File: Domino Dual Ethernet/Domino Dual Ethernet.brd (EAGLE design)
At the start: 45.7 x 33 mm, 47 parts, among them J1 HL-59T-2X1, J2 MH18-1, J3 MH18-1

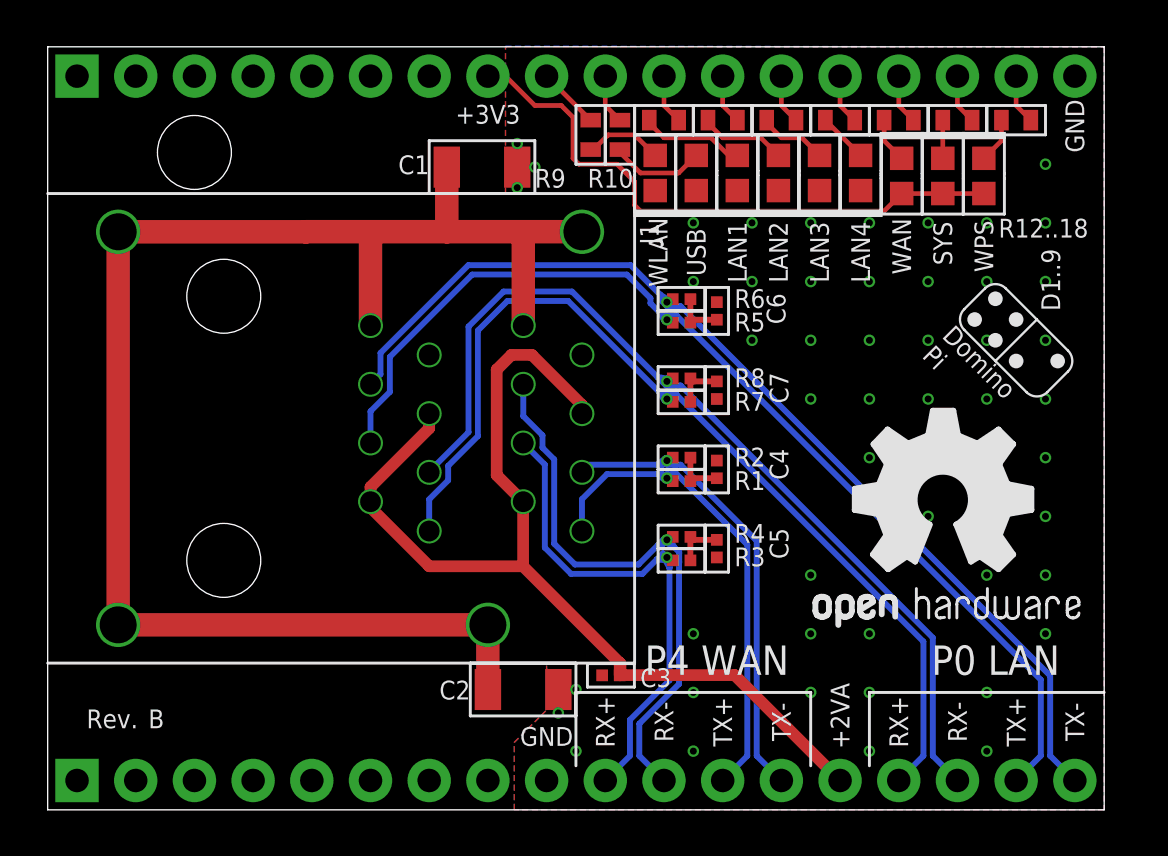
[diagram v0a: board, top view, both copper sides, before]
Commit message: Domino Dual Ethernet Rev. C: Changed dual Magjack connector for new one, changed Logos
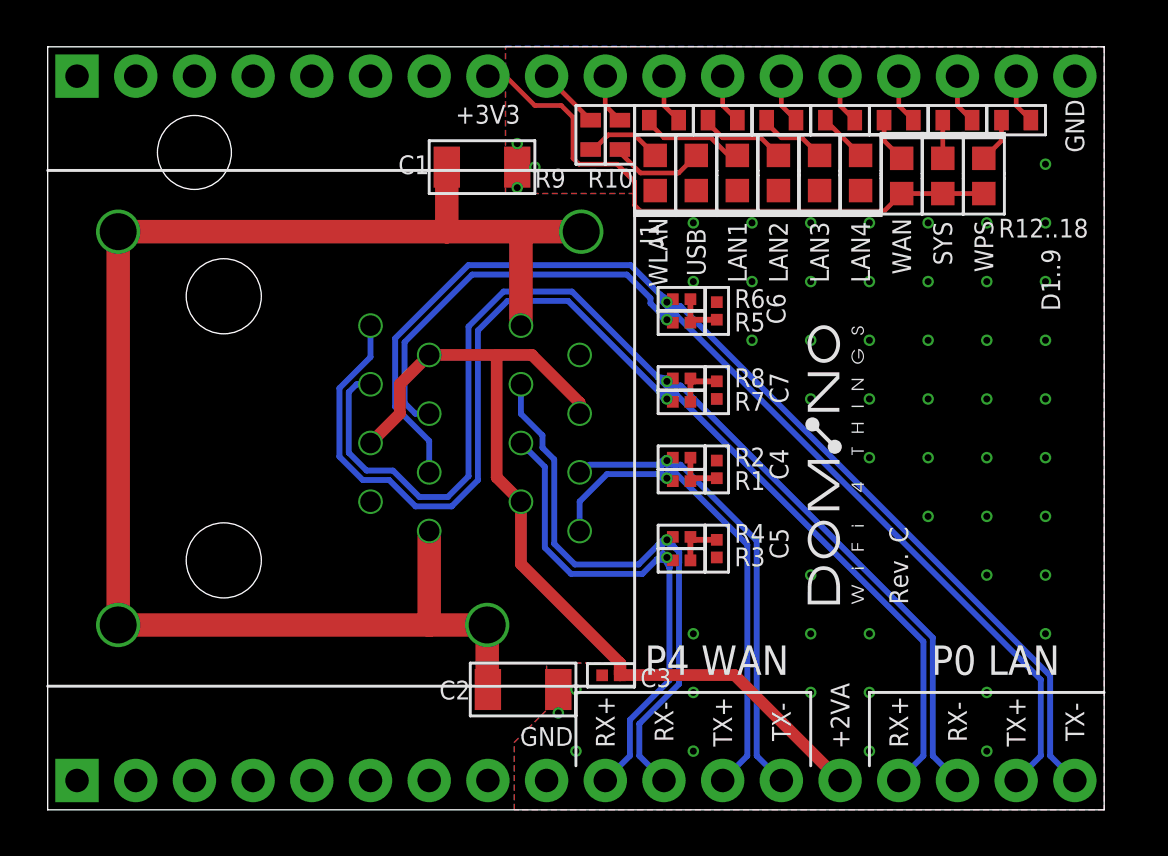
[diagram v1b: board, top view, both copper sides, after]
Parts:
- removed U$13: (no value), Domino:DOMINO_LOGO_SMALL
- removed U$16: (no value), Domino:OPEN_HARDWARE_LOGO
- added U$10: DOMINO_LOGO, Domino:DOMINO_LOGO
- added U$11: (no value), Domino:DOMINO_LOGO_SMALL
- J1: value HL-59T-2X1 -> HBJ-2H101NLF; device Domino:HL-59T-2X1 -> Domino:HBJ-2H101NLF
- moved U$6 19.7 mm to (14.6, 22.2)
- moved U$5 19.4 mm to (21.6, 22.2)
- moved U$7 17.3 mm to (14.0, 8.26)
- moved U$4 3.86 mm to (43.2, 15.2), turned to 0 degrees
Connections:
- net +2VA_ETH_OUT: now also J1.DN2, J1.DN5; no longer J1.DP2, J1.DP5
- net P0_RX_N: now also J1.DN3; no longer J1.DP3
- net P0_RX_P: now also J1.DN1; no longer J1.DP1
- net P0_TX_N: now also J1.DN6; no longer J1.DP6
- net P0_TX_P: now also J1.DN4; no longer J1.DP4
- net SHIELD: now also J1.DN8; no longer J1.DP8
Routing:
- net P0_RX_P: track 44.7 -> 55.2 mm
- net P0_RX_N: track 43.3 -> 52.8 mm
- net +2VA_ETH_OUT: track 45.4 -> 40.7 mm
- net P0_TX_N: track 47.3 -> 51.2 mm
- net P0_TX_P: track 48.7 -> 47.6 mm
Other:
- board text removed: "Domino Core"
- board text removed: "Domino Pi"
- board text removed: "Domino Qi"

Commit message: Domino Dual Ethernet Rev. D: changed silkscreen font ratio to 20%
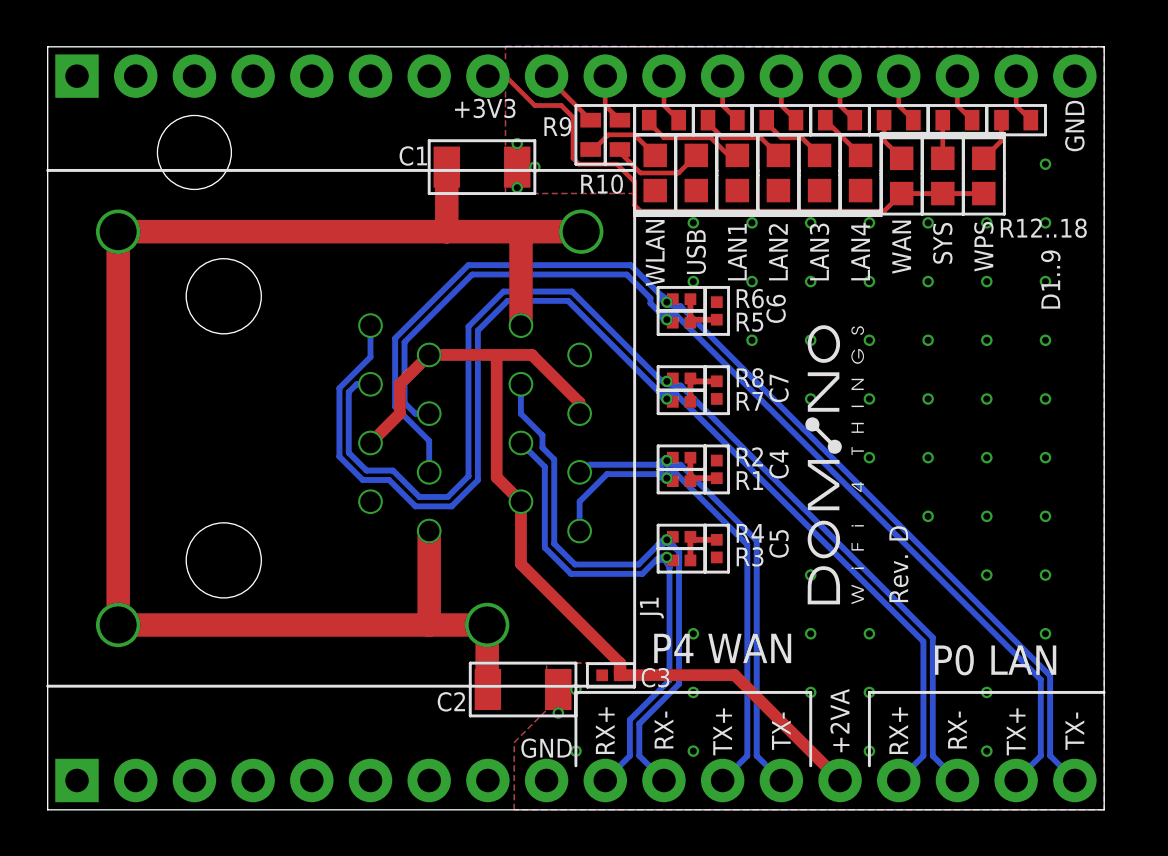
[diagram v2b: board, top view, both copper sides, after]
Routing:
- net P0_RX_N: track 52.8 -> 50.5 mm
- net P0_TX_N: track 51.2 -> 50.0 mm
- net P4_RX_P: track 24.5 -> 23.9 mm

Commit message: Added UART header to both Ethernet tiles
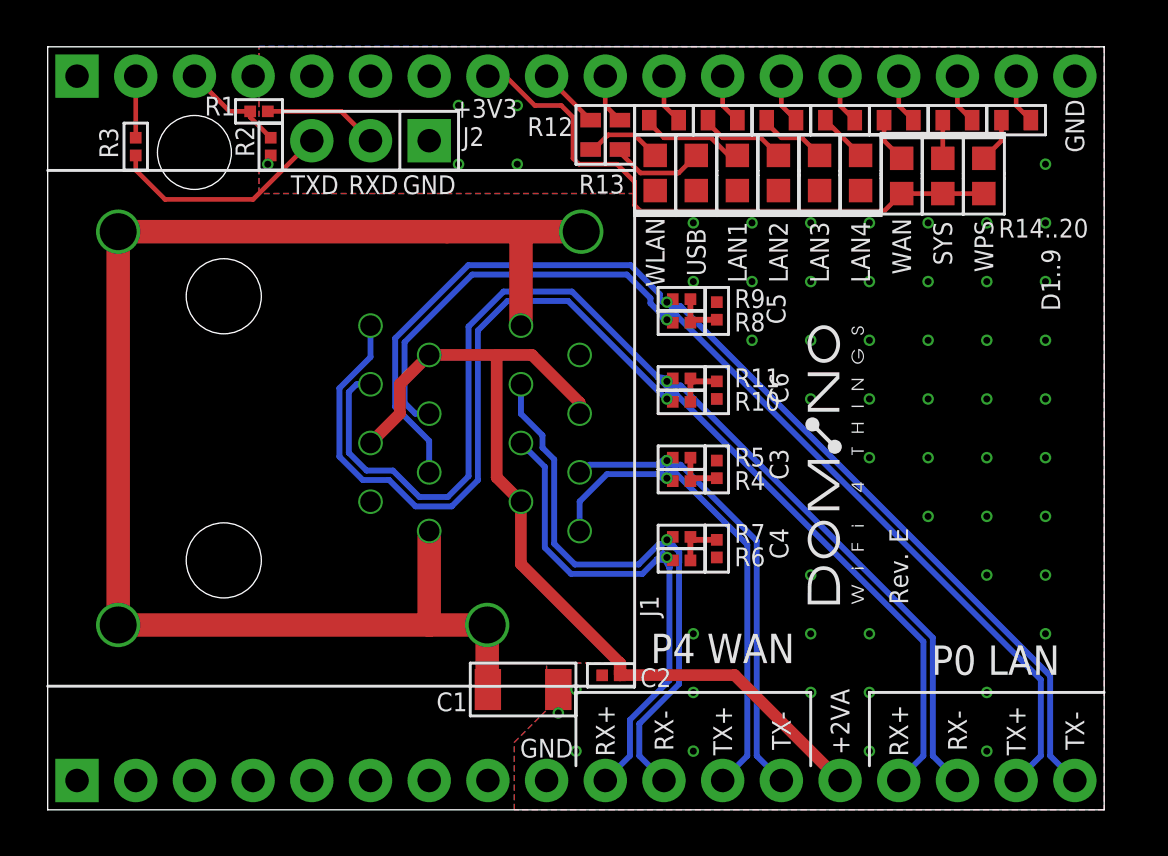
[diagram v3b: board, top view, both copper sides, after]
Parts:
- removed C7: 100n, Domino:C0402
- added J4: MH18-1, Domino:MH18-1-0.1
- added R18, R19, R20: 330R, Domino:R0603
- C2: value 2n2 -> 100n; device Domino:C1206 -> Domino:C0402
- J2: value MH18-1 -> MH3-1; device Domino:MH18-1-0.1 -> Domino:MH3-1-0.1
- R1: value 49R9 -> 4k7
- R10, R11, R9: value 270R -> 49R9; device Domino:R0603 -> Domino:R0402
- R15, R16, R17: value 330R -> 270R
- R2: value 49R9 -> 15k
- R3: value 49R9 -> 220R
- moved J3 30.5 mm to (1.27, 31.8)
- moved R3 29.6 mm to (3.81, 28.7), turned to 90 degrees
- moved R1 24.3 mm to (9.14, 30.2)
- moved C1 22.7 mm to (20.6, 5.21)
- moved R2 22.3 mm to (9.65, 28.7), turned to 270 degrees
- moved J2 13.0 mm to (14.0, 29.0), flipped to the top
- moved R10 11.9 mm to (27.4, 17.7), turned to 180 degrees
- moved R6 11.3 mm to (27.4, 10.8)
- moved R11 11.2 mm to (27.4, 18.7)
- moved C5 10.3 mm to (29.0, 21.6), turned to 270 degrees
- moved C3 10.0 mm to (29.0, 14.7), turned to 270 degrees
- moved R9 8.13 mm to (27.4, 22.1), turned to 180 degrees
- moved R14 7.62 mm to (26.7, 29.8)
- moved R15 7.62 mm to (29.2, 29.8)
- moved R16 7.62 mm to (31.8, 29.8)
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- renumbered U$10 to L1
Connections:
- new net RXD: J2.2, R1.1
- new net TXD: J2.3, R3.1
- new net UART_RX: J3.3, R1.2, R2.1
- new net UART_TX: J3.2, R3.2
- net +2VA_ETH_OUT: now also C2.2, J4.14; no longer C3.2, J3.14
- net +3V3: now also J3.8; no longer J2.8
- net GND: now also J2.1, J3.18, J4.9, R2.2; no longer C7.1, J2.18, J3.9
- net LAN1_LED: now also R14.2; no longer R11.2
- net LAN2_LED: now also R15.2; no longer R12.2
- net LAN3_LED: now also R16.2; no longer R13.2
- net LAN4_LED: now also R17.2; no longer R14.2
- net LED0: now also J3.9, R12.1; no longer J2.9, R9.1
- net LED1: now also J3.10, R13.1; no longer J2.10, R10.1
- net LED2: now also J3.11, R14.1; no longer J2.11, R11.1
- net LED3: now also J3.12, R15.1; no longer J2.12, R12.1
- net LED4: now also J3.13, R16.1; no longer J2.13, R13.1
- net LED5: now also J3.14, R17.1; no longer J2.14, R14.1
- net LED6: now also J3.15, R18.1; no longer J2.15, R15.1
- net LED7: now also J3.16, R19.1; no longer J2.16, R16.1
- net LED8: now also J3.17, R20.1; no longer J2.17, R17.1
- net P0_RX: now also C6.2, R10.1, R11.1; no longer C7.2, R7.1, R8.1
- net P0_RX_N: now also J4.16, R11.2; no longer J3.16, R8.2
- net P0_RX_P: now also J4.15, R10.2; no longer J3.15, R7.2
- net P0_TX: now also C5.2, R8.1, R9.1; no longer C6.2, R5.1, R6.1
- net P0_TX_N: now also J4.18, R9.2; no longer J3.18, R6.2
- net P0_TX_P: now also J4.17, R8.2; no longer J3.17, R5.2
- net P4_RX: now also C4.2, R6.1, R7.1; no longer C5.2, R3.1, R4.1
- net P4_RX_N: now also J4.11, R7.2; no longer J3.11, R4.2
- net P4_RX_P: now also J4.10, R6.2; no longer J3.10, R3.2
- net P4_TX: now also C3.2, R4.1, R5.1; no longer C4.2, R1.1, R2.1
- net P4_TX_N: now also J4.13, R5.2; no longer J3.13, R2.2
- net P4_TX_P: now also J4.12, R4.2; no longer J3.12, R1.2
- net SHIELD: no longer C2.2
- net SYS_LED: now also R19.2; no longer R16.2
- net USB_LED: now also R13.2; no longer R10.2
- net WAN_LED: now also R18.2; no longer R15.2
- net WLAN_LED: now also R12.2; no longer R9.2
- net WPS_LED: now also R20.2; no longer R17.2
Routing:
- net TXD: track 0.00 -> 9.83 mm
- net RXD: track 0.00 -> 4.97 mm
- net UART_RX: track 0.00 -> 4.56 mm
- net SHIELD: track 66.8 -> 64.0 mm
- net UART_TX: track 0.00 -> 2.67 mm
- net P0_RX_N: track 50.5 -> 52.8 mm
- net P0_TX_N: track 50.0 -> 48.8 mm
- net P0_RX_P: track 55.2 -> 54.1 mm
- net P4_RX_N: track 27.5 -> 26.4 mm
- net P4_RX_P: track 23.9 -> 24.5 mm
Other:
- board text added: "R14..20"
- board text added: "RXD"
- board text added: "TXD"
- board text added: "UART_RX"
- board text added: "UART_TX"
- board text removed: "R12..18"
